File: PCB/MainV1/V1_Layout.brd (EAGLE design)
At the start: 160 x 100 mm, 22 parts, among them IC3 AD623R, U2 MB85RC256VPF-G-JNERE2

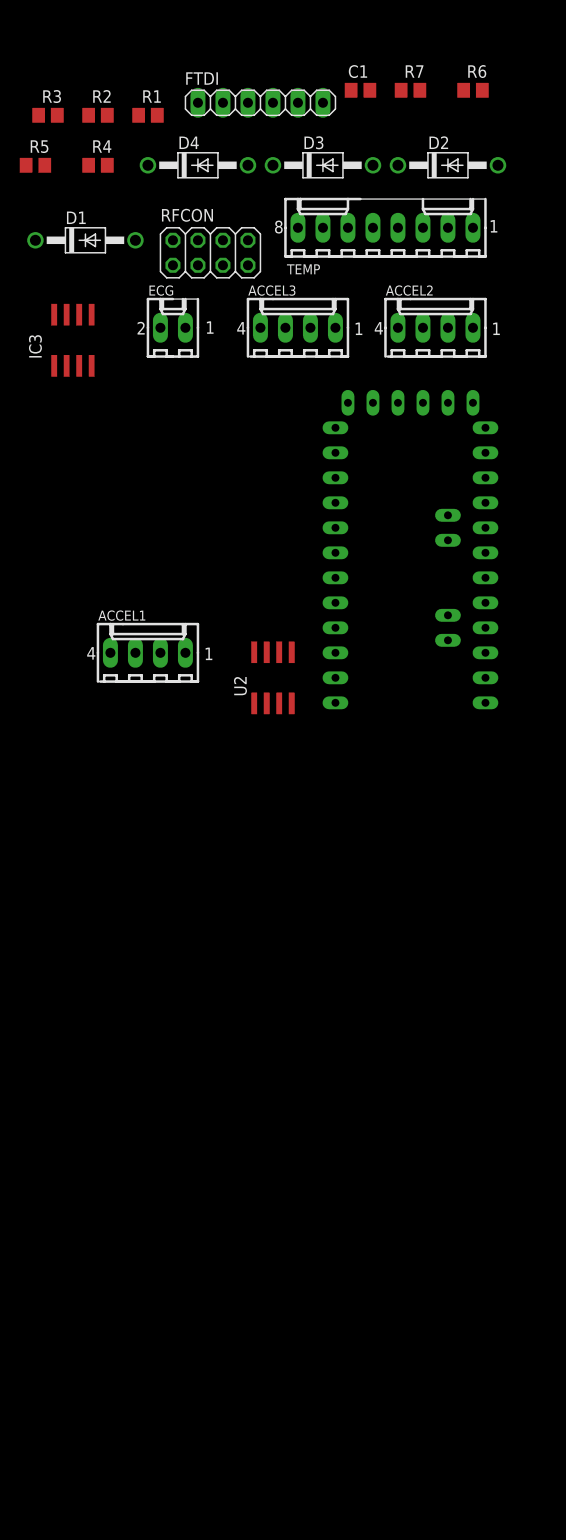
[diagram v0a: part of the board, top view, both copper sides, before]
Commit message: working on schematic, and first commit of temperature buddy board
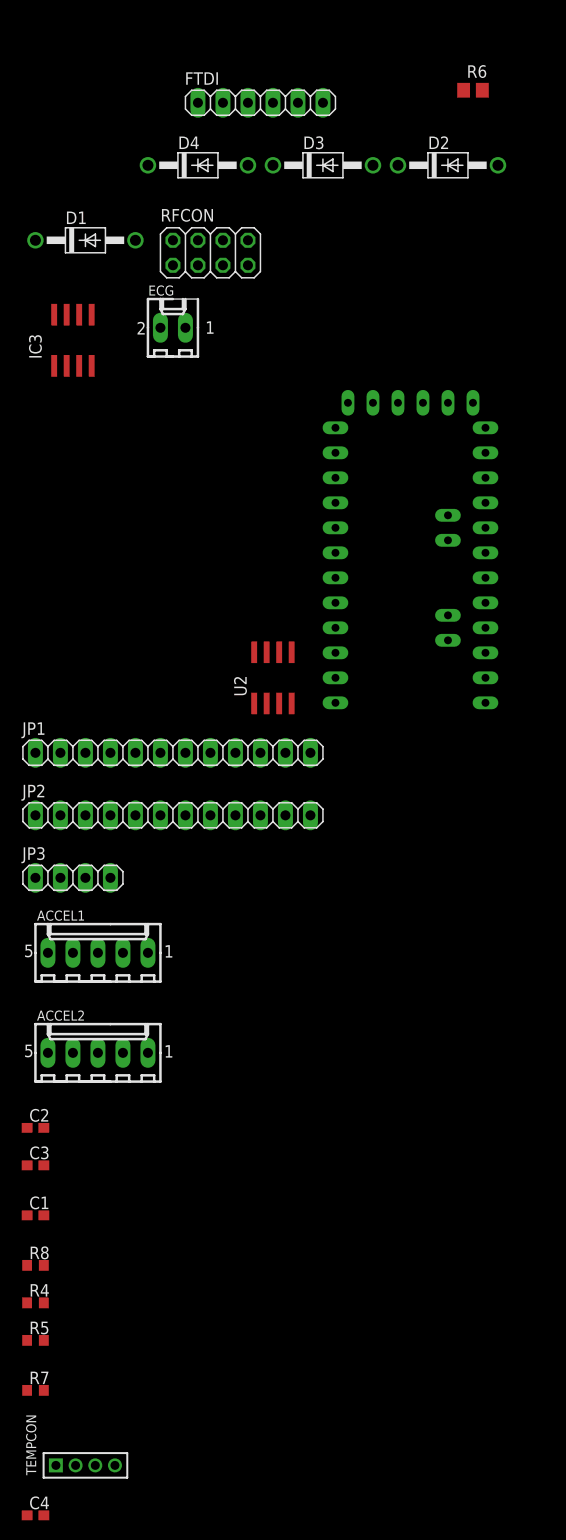
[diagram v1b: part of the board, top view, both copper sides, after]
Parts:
- removed ACCEL3: 22-27-2041-04, con-molex:6410-04
- removed R1, R2, R3: (no value), rcl:R0805
- removed TEMP: 22-27-2081-08, con-molex:6410-08
- added C2, C3, C4: 1uF, rcl:C0603
- added JP1, JP2: (no value), pinhead:1X12
- added JP3: (no value), pinhead:1X04
- added R8: (no value), rcl:R0603
- added TEMPCON: (no value), pinhead2:1X04M
- ACCEL1, ACCEL2: value 22-27-2041-04 -> 22-27-2051-05; device con-molex:6410-04 -> con-molex:6410-05
- C1: device rcl:C0805 -> rcl:C0603
- R4, R5, R7: device rcl:R0805 -> rcl:R0603
- moved R7 137.5 mm to (-61.0, -68.6)
- moved R5 119.4 mm to (-61.0, -63.5)
- moved C1 119.0 mm to (-61.0, -50.8)
- moved R4 115.7 mm to (-61.0, -59.7)
- moved ACCEL2 81.3 mm to (-54.6, -34.3)
- moved ACCEL1 30.9 mm to (-54.6, -24.1)
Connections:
- removed net A0: ACCEL3.4, TEMP.5
- removed net A1: TEMP.6
- removed net A2: TEMP.7
- removed net N$15: FTDI.3, U$1.VCC1
- removed net OS: R3.2, TEMP.4
- new net N$10: JP1.11, U$1.RX1
- new net N$11: JP1.10, U$1.RST1
- new net N$17: JP1.8, U$1.D2
- new net N$18: JP1.7, U$1.D3
- new net N$19: JP1.6, U$1.D4
- new net N$20: JP1.5, U$1.D5
- new net N$21: JP2.1, U$1.RAW
- new net N$23: JP2.3, U$1.RST
- new net N$24: JP2.5, U$1.A3
- new net N$25: JP2.6, U$1.A2
- new net N$26: JP2.7, U$1.A1
- new net N$27: JP2.8, U$1.A0
- new net N$28: JP3.4, U$1.A6
- new net N$29: JP3.3, U$1.A7
- new net N$9: JP1.12, U$1.TX0
- net +3V3: now also ACCEL1.1, ACCEL1.5, ACCEL2.1, C1.1, C2.1, C4.1, FTDI.3, JP2.4, TEMPCON.1, U$1.VCC1
- net D10: now also JP2.12
- net D11: now also JP2.11
- net D12: now also JP2.10
- net D13: now also JP2.9
- net D6: now also JP1.4
- net D7: now also JP1.3
- net D8: now also JP1.2
- net D9: now also JP1.1
- net GND: now also ACCEL1.2, ACCEL2.2, ACCEL2.5, C2.2, C3.2, C4.2, JP1.9, JP2.2, TEMPCON.4; no longer ACCEL1.4, ACCEL2.4, TEMP.8
- net N$2: now also R5.2; no longer R5.1
- net N$4: now also R5.1; no longer R5.2
- net N$6: now also C3.1; no longer C1.1
- net SCL: now also JP3.1, TEMPCON.3; no longer R2.2, TEMP.3
- net SDA: now also ACCEL1.4, ACCEL2.4, JP3.2, TEMPCON.2; no longer ACCEL1.2, ACCEL2.2, R1.2, TEMP.2
- net VCC: no longer ACCEL1.1, ACCEL2.1, R1.1, R2.1, R3.1, TEMP.1

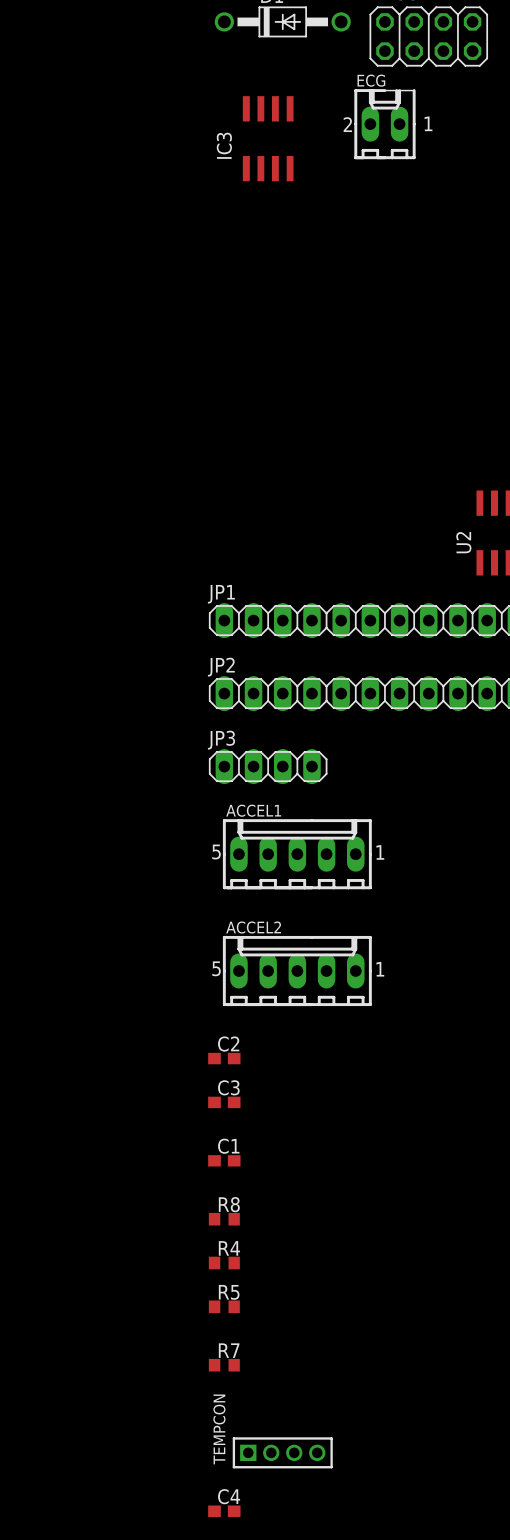
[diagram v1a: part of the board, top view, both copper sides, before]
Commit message: Changes ready for digital schematic design review (ECG STILL TODO)
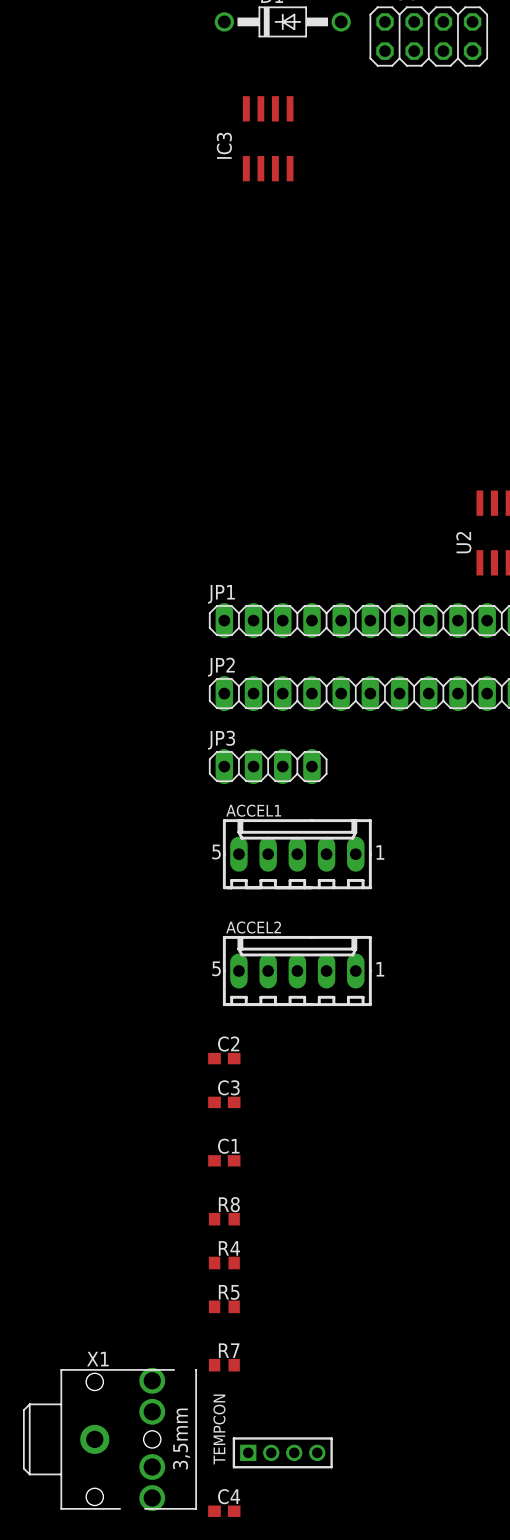
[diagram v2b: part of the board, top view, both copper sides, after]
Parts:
- removed ECG: 22-27-2021-02, con-molex:6410-02
- added X1: STEREOJACK, adafruit:STX3100
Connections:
- new net ECG-L: X1.1
- new net ECG-R: X1.5
- new net ECG-REF: X1.2
- net N$1: no longer ECG.1
- net N$4: no longer ECG.2
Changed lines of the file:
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@@
 <attribute name="VALUE" x="-46.482" y="53.086" size="1.27" layer="27" ratio="10"/>
-</element>
-<element name="ECG" library="con-molex" library_urn="urn:adsk.eagle:library:165" package="6410-02" value="22-27-2021-02" x="-46.99" y="39.37" smashed="yes">
-<attribute name="MF" value="MOLEX" x="0" y="0" size="1.778" layer="27" display="off"/>
-<attribute name="MPN" value="" x="0" y="0" size="1.778" layer="27" display="off"/>
-<attribute name="NAME" x="-49.5031" y="42.6451" size="1.016" layer="25" ratio="10"/>
-<attribute name="OC_FARNELL" value="unknown" x="0" y="0" size="1.778" layer="27" display="off"/>
-<attribute name="OC_NEWARK" value="unknown" x="0" y="0" size="1.778" layer="27" display="off"/>
-<attribute name="VALUE" x="-49.5031" y="34.7711" size="0.8128" layer="27" ratio="10"/>
 </element>
 <element name="FTDI" library="pinhead" library_urn="urn:adsk.eagle:library:325" package="1X06" package3d_urn="urn:adsk.eagle:package:22472/2" value="" x="-38.1" y="62.23" smashed="yes">
@@
 <attribute name="SPICEPREFIX" value="C" x="-60.96" y="-81.28" size="1.778" layer="27" display="off"/>
 <attribute name="VALUE" x="-61.595" y="-83.185" size="1.27" layer="27"/>
+</element>
+<element name="X1" library="adafruit" package="STX3100" value="STEREOJACK" x="-74.93" y="-74.93" smashed="yes">
+<attribute name="NAME" x="-72.945" y="-68.68" size="1.27" layer="25" ratio="10"/>
+<attribute name="VALUE" x="-73.58" y="-82.65" size="1.27" layer="27" ratio="10"/>
 </element>
 </elements>
@@
 </signal>
 <signal name="N$1">
-<contactref element="ECG" pad="1"/>
 <contactref element="R4" pad="1"/>
-<wire x1="-45.72" y1="39.37" x2="-61.81" y2="-59.69" width="0" layer="19" extent="1-1"/>
 </signal>
 <signal name="N$4">
-<contactref element="ECG" pad="2"/>
 <contactref element="R5" pad="1"/>
-<wire x1="-48.26" y1="39.37" x2="-61.81" y2="-63.5" width="0" layer="19" extent="1-1"/>
 </signal>
 <signal name="N$2">
@@
 <wire x1="-19.05" y1="10.16" x2="-55.88" y2="-16.51" width="0" layer="19" extent="1-1"/>
 </signal>
+<signal name="ECG-L">
+<contactref element="X1" pad="1"/>
+</signal>
+<signal name="ECG-R">
+<contactref element="X1" pad="5"/>
+</signal>
+<signal name="ECG-REF">
+<contactref element="X1" pad="2"/>
+</signal>
 </signals>

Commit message: main schematic ready for review
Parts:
- added D5, D6: (no value), diode:DO35-7
- added D7, D8: 1N4004, diode:DO41-10
- added IC1: AD826N, analog-devices:DIL08
- added PWR: (no value), pinhead:1X02
- added R1, R2: 100k, rcl:R0603
- added R3: 330k, rcl:R0603
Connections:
- removed net N$1: R4.1
- removed net N$27: JP2.8, U$1.A0
- removed net N$4 (its old number): R5.1
- removed net VCC: IC3.7
- new net A0: C3.2, D5.C, D6.A, JP2.8, R7.2, U$1.A0
- new net N$3: IC1.3, R1.1, R2.2
- net +3V3: now also D6.C, IC1.8, IC3.7, R1.2
- net AGND: now also D7.C, D8.A, IC1.1, IC1.2, R3.2
- net ECG-L: now also R4.1
- net ECG-R: now also R5.1
- net ECG-REF: now also R3.1
- net GND: now also D5.A, D7.A, D8.C, IC1.4, IC1.5, IC1.6, PWR.1, R2.1; no longer C3.2, R7.2
- net N$21: now also PWR.2

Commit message: Schematic cleanup, added bypass caps, added inndicator LEDs
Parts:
- added C10: (no value), rcl:E3,5-8
- added C11, C8, C9: (no value), rcl:C025-030X050
- added C5, C7: 1uF, rcl:C0603
- added C6: 100nF, rcl:C0603
- added IND1, IND2, IND3, PWR1: (no value), led:CHIPLED_0805
- added R10, R9: 10k, rcl:R0603
- added R11, R12, R13: 150R, rcl:R0603
- R8: value (none) -> 150R
- moved PWR 235.9 mm to (-16.5, 74.9)
- moved D6 218.7 mm to (-61.0, 85.1)
- moved D5 214.6 mm to (-49.5, 85.1)
- moved R3 205.9 mm to (-43.2, 81.3)
- moved D8 203.9 mm to (-44.5, 55.9)
- moved D7 198.5 mm to (-31.8, 55.9)
- moved R2 188.3 mm to (-36.8, 81.3)
- moved R1 186.0 mm to (-30.5, 81.3)
- moved C4 171.1 mm to (-26.7, 86.4)
- moved R7 149.9 mm to (-62.2, 81.3)
- moved R5 144.9 mm to (-55.9, 81.3)
- moved R4 141.4 mm to (-49.5, 81.3)
- moved C3 137.8 mm to (-21.6, 86.4)
- moved C2 135.8 mm to (-16.5, 86.4)
- moved C1 132.6 mm to (-72.4, 81.3)
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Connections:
- removed net N$18: JP1.7, U$1.D3
- removed net N$19: JP1.6, U$1.D4
- removed net N$20: JP1.5, U$1.D5
- new net D3: IND1.A, JP1.7, U$1.D3
- new net D4: IND2.A, JP1.6, U$1.D4
- new net D5: IND3.A, JP1.5, U$1.D5
- new net N$1: PWR1.C, R11.2
- new net N$14: IND1.C, R8.2
- new net N$15: IND2.C, R12.2
- new net N$16: IND3.C, R13.2
- net +3V3: now also C10.+, C11.1, C5.2, C6.1, C7.1, C8.1, C9.1, PWR1.A, R10.2, R9.2
- net GND: now also C10.-, C11.2, C5.1, C6.2, C7.2, C8.2, C9.2, R11.1, R12.1, R13.1, R8.1
- net SCL: now also R9.1
- net SDA: now also R10.1

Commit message: Review changes complete. Starting layout
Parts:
- removed D7, D8: 1N4004, diode:DO41-10
- C10: value (none) -> 10uF
- C11, C9: value (none) -> 1uF
- C7: value 1uF -> 10nF
- C8: value (none) -> 100nF
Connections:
- net AGND: no longer D7.C, D8.A
- net D6: no longer U2.3
- net D7: no longer U2.2
- net D8: no longer U2.1
- net GND: now also U2.1, U2.2, U2.3; no longer D7.A, D8.C

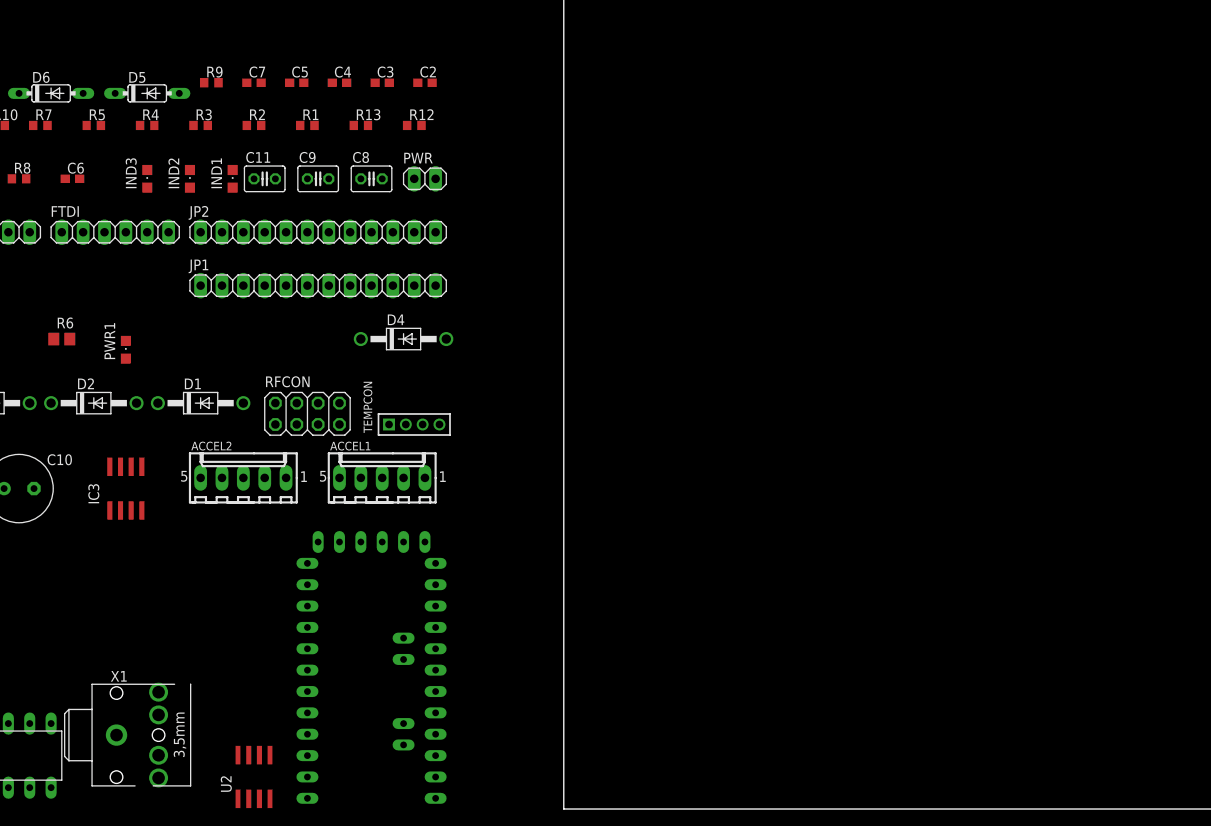
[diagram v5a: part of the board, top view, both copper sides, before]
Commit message: Finished routing Temp Buddy Board. Please review.
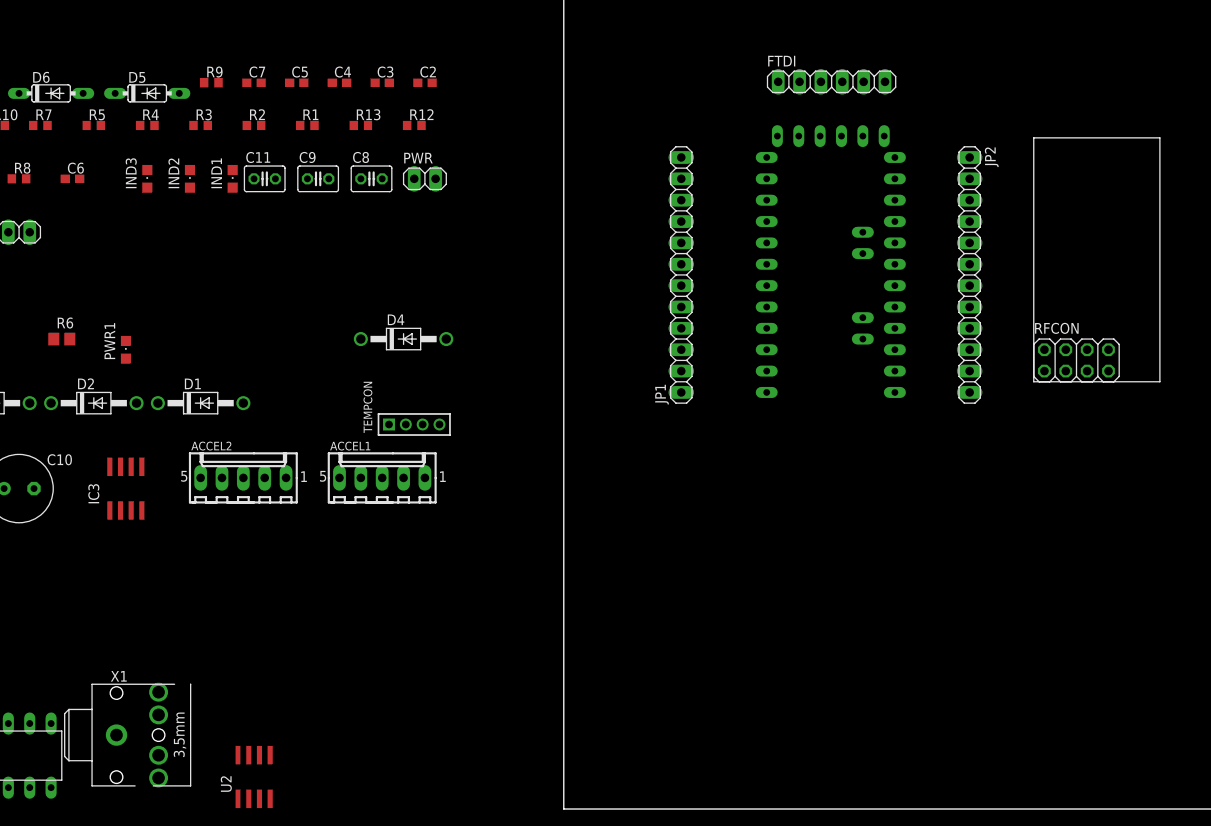
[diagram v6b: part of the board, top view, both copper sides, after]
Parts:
- RFCON: value (none) -> NRF24L01_MODULE; device pinhead:2X04 -> Custom Parts:2X04
- moved FTDI 87.0 mm to (31.8, 86.5)
- moved RFCON 86.4 mm to (55.9, 50.8)
- moved JP2 77.6 mm to (48.3, 63.5), turned to 270 degrees
- moved U$1 72.9 mm to (33.0, 64.8)
- moved JP1 43.2 mm to (14.0, 63.5), turned to 90 degrees
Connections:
- net A0: now also U$1.A3; no longer U$1.A0
- net N$24: now also U$1.A0; no longer U$1.A3
- net N$25: now also U$1.A1; no longer U$1.A2
- net N$26: now also U$1.A2; no longer U$1.A1
